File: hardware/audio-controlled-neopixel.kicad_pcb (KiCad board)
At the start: 2 copper layers, 96 x 56 mm, 61 parts, among them J1 Phoenix MPT, J2 KF2EDGK, J3 KF2EDGK, J4 KF2EDGK, J5 Conn_01x01_Female, J6 Conn_01x01_Female, J7 Conn_01x01_Female, J8 Conn_01x01_Female, SW1 SW_SPST, U1 LM324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

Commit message: minor PCB clean up
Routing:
- net -12V: track 198.4 -> 204.7 mm
- net Net-(C2-Pad1): track 23.4 -> 24.6 mm
- net +12V: track 138.8 -> 139.8 mm
- net Net-(C1-Pad1): track 29.2 -> 29.8 mm
- net /Buf_input: track 35.6 -> 36.1 mm
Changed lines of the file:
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@@
     (thickness 1.6)
     (drawings 23)
-    (tracks 331)
+    (tracks 326)
     (zones 0)
     (modules 61)
@@
   (segment (start 48.26 51.308) (end 48.26 52.672) (width 0.5) (layer F.Cu) (net 2))
   (segment (start 48.006 51.054) (end 48.26 51.308) (width 0.5) (layer F.Cu) (net 2))
-  (segment (start 44.102 52.672) (end 46.99 52.672) (width 0.5) (layer F.Cu) (net 2))
-  (segment (start 41.148 67.818) (end 41.148 55.626) (width 0.5) (layer F.Cu) (net 2))
-  (segment (start 41.148 55.626) (end 44.102 52.672) (width 0.5) (layer F.Cu) (net 2))
+  (segment (start 42.07 52.672) (end 46.99 52.672) (width 0.5) (layer F.Cu) (net 2))
+  (segment (start 41.148 67.818) (end 41.148 53.594) (width 0.5) (layer F.Cu) (net 2))
+  (segment (start 41.148 53.594) (end 42.07 52.672) (width 0.5) (layer F.Cu) (net 2))
   (segment (start 54.61 52.672) (end 54.61 51.422) (width 0.5) (layer F.Cu) (net 3))
   (segment (start 53.34 51.422) (end 53.708 51.054) (width 0.5) (layer F.Cu) (net 3))
@@
   (segment (start 46.736 66.518) (end 43.434 63.216) (width 0.5) (layer F.Cu) (net 3))
   (segment (start 46.736 67.818) (end 46.736 66.518) (width 0.5) (layer F.Cu) (net 3))
-  (segment (start 43.434 63.216) (end 43.434 56.134) (width 0.5) (layer F.Cu) (net 3))
-  (segment (start 43.434 56.134) (end 45.212 54.356) (width 0.5) (layer F.Cu) (net 3))
-  (segment (start 45.212 54.356) (end 52.906 54.356) (width 0.5) (layer F.Cu) (net 3))
+  (segment (start 43.434 63.216) (end 43.434 55.118) (width 0.5) (layer F.Cu) (net 3))
+  (segment (start 43.434 55.118) (end 44.196 54.356) (width 0.5) (layer F.Cu) (net 3))
+  (segment (start 44.196 54.356) (end 52.906 54.356) (width 0.5) (layer F.Cu) (net 3))
   (segment (start 52.906 54.356) (end 53.34 53.922) (width 0.5) (layer F.Cu) (net 3))
   (segment (start 67.915 58.674) (end 67.945 58.704) (width 0.5) (layer F.Cu) (net 4))
@@
   (segment (start 46.9085 57.9905) (end 46.99 58.072) (width 0.5) (layer F.Cu) (net 5))
   (segment (start 44.958 57.9905) (end 46.9085 57.9905) (width 0.5) (layer F.Cu) (net 5))
-  (segment (start 61.6435 55.5475) (end 61.6435 56.896) (width 0.5) (layer F.Cu) (net 5))
-  (segment (start 61.214 55.118) (end 61.6435 55.5475) (width 0.5) (layer F.Cu) (net 5))
-  (segment (start 48.694 55.118) (end 61.214 55.118) (width 0.5) (layer F.Cu) (net 5))
-  (segment (start 46.99 58.072) (end 46.99 56.822) (width 0.5) (layer F.Cu) (net 5))
-  (segment (start 46.99 56.822) (end 48.694 55.118) (width 0.5) (layer F.Cu) (net 5))
   (segment (start 65.913 56.896) (end 66.04 57.023) (width 0.5) (layer F.Cu) (net 5))
   (segment (start 61.6435 56.896) (end 65.913 56.896) (width 0.5) (layer F.Cu) (net 5))
+  (segment (start 61.6435 55.5475) (end 61.6435 56.896) (width 0.5) (layer F.Cu) (net 5))
+  (segment (start 61.214 55.118) (end 61.6435 55.5475) (width 0.5) (layer F.Cu) (net 5))
+  (segment (start 47.752 55.118) (end 61.214 55.118) (width 0.5) (layer F.Cu) (net 5))
+  (segment (start 46.99 58.072) (end 46.99 55.88) (width 0.5) (layer F.Cu) (net 5))
+  (segment (start 46.99 55.88) (end 47.752 55.118) (width 0.5) (layer F.Cu) (net 5))
   (segment (start 83.057 83.7385) (end 83.1065 83.788) (width 0.5) (layer F.Cu) (net 6))
   (segment (start 83.057 81.375) (end 83.057 83.7385) (width 0.5) (layer F.Cu) (net 6))
@@
   (segment (start 79.248 70.9445) (end 79.248 69.85) (width 0.5) (layer F.Cu) (net 21))
   (segment (start 79.248 69.85) (end 79.248 67.978) (width 0.5) (layer F.Cu) (net 21))
-  (via (at 63.246 30.734) (size 0.8) (drill 0.4) (layers F.Cu B.Cu) (net 21))
   (segment (start 39.37 42.164) (end 50.8 30.734) (width 0.5) (layer B.Cu) (net 21))
   (segment (start 39.37 56.388) (end 39.37 42.164) (width 0.5) (layer B.Cu) (net 21))
@@
   (segment (start 62.680315 30.734) (end 63.246 30.734) (width 0.5) (layer B.Cu) (net 21))
   (via (at 77.47 73.152) (size 0.8) (drill 0.4) (layers F.Cu B.Cu) (net 21))
-  (segment (start 63.645999 31.133999) (end 63.246 30.734) (width 0.5) (layer F.Cu) (net 21))
-  (segment (start 69.088 37.338) (end 69.088 39.116) (width 0.5) (layer F.Cu) (net 21))
-  (segment (start 68.326 39.878) (end 64.77 39.878) (width 0.5) (layer F.Cu) (net 21))
-  (segment (start 64.77 39.878) (end 64.262 39.37) (width 0.5) (layer F.Cu) (net 21))
-  (segment (start 64.262 39.37) (end 64.262 31.75) (width 0.5) (layer F.Cu) (net 21))
-  (segment (start 64.262 31.75) (end 63.645999 31.133999) (width 0.5) (layer F.Cu) (net 21))
-  (segment (start 115.824 34.414208) (end 115.445792 34.036) (width 0.5) (layer F.Cu) (net 21))
-  (segment (start 115.824 35.687) (end 115.824 34.414208) (width 0.5) (layer F.Cu) (net 21))
-  (segment (start 115.445792 34.036) (end 80.518 34.036) (width 0.5) (layer F.Cu) (net 21))
-  (segment (start 80.518 34.036) (end 74.676 39.878) (width 0.5) (layer F.Cu) (net 21))
-  (segment (start 69.088 39.116) (end 69.088 39.878) (width 0.5) (layer F.Cu) (net 21))
-  (segment (start 74.676 39.878) (end 69.088 39.878) (width 0.5) (layer F.Cu) (net 21))
-  (segment (start 69.088 39.878) (end 68.326 39.878) (width 0.5) (layer F.Cu) (net 21))
   (segment (start 39.37 72.898) (end 39.37 56.388) (width 0.5) (layer B.Cu) (net 21))
   (segment (start 50.8 84.328) (end 39.37 72.898) (width 0.5) (layer B.Cu) (net 21))
@@
   (segment (start 79.248 70.9445) (end 77.6455 70.9445) (width 0.5) (layer F.Cu) (net 21))
   (segment (start 77.6455 70.9445) (end 77.47 71.12) (width 0.5) (layer F.Cu) (net 21))
+  (segment (start 115.824 31.242) (end 115.824 35.687) (width 0.5) (layer B.Cu) (net 21))
+  (segment (start 115.316 30.734) (end 115.824 31.242) (width 0.5) (layer B.Cu) (net 21))
+  (via (at 74.422 30.734) (size 0.8) (drill 0.4) (layers F.Cu B.Cu) (net 21))
+  (segment (start 63.246 30.734) (end 74.422 30.734) (width 0.5) (layer B.Cu) (net 21))
+  (segment (start 74.422 30.734) (end 115.316 30.734) (width 0.5) (layer B.Cu) (net 21))
+  (segment (start 74.422 38.862) (end 74.422 30.734) (width 0.5) (layer F.Cu) (net 21))
+  (segment (start 73.152 40.132) (end 74.422 38.862) (width 0.5) (layer F.Cu) (net 21))
+  (segment (start 69.85 40.132) (end 73.152 40.132) (width 0.5) (layer F.Cu) (net 21))
+  (segment (start 69.088 37.338) (end 69.088 39.37) (width 0.5) (layer F.Cu) (net 21))
+  (segment (start 69.088 39.37) (end 69.85 40.132) (width 0.5) (layer F.Cu) (net 21))
   (segment (start 50.8 50.7215) (end 50.8 52.672) (width 0.5) (layer F.Cu) (net 22))
   (segment (start 50.8 48.9435) (end 50.8 50.7215) (width 0.5) (layer F.Cu) (net 22))
-  (segment (start 65.278 37.338) (end 66.548 37.338) (width 0.5) (layer B.Cu) (net 22))
-  (segment (start 109.471208 35.687) (end 105.534208 31.75) (width 0.5) (layer B.Cu) (net 22))
-  (segment (start 110.744 35.687) (end 109.471208 35.687) (width 0.5) (layer B.Cu) (net 22))
-  (segment (start 105.534208 31.75) (end 65.786 31.75) (width 0.5) (layer B.Cu) (net 22))
   (segment (start 65.786 31.75) (end 64.516 33.02) (width 0.5) (layer B.Cu) (net 22))
-  (segment (start 64.516 33.02) (end 64.516 36.576) (width 0.5) (layer B.Cu) (net 22))
-  (segment (start 64.516 36.576) (end 65.278 37.338) (width 0.5) (layer B.Cu) (net 22))
-  (segment (start 66.548 37.338) (end 66.548 39.624) (width 0.5) (layer B.Cu) (net 22))
   (via (at 50.8 50.7215) (size 0.8) (drill 0.4) (layers F.Cu B.Cu) (net 22))
   (segment (start 40.5615 50.7215) (end 50.8 50.7215) (width 0.5) (layer B.Cu) (net 22))
@@
   (segment (start 78.0265 59.7385) (end 77.47 59.182) (width 0.5) (layer F.Cu) (net 22))
   (segment (start 77.47 59.182) (end 77.47 56.896) (width 0.5) (layer F.Cu) (net 22))
-  (segment (start 70.104 43.18) (end 70.104 55.372) (width 0.5) (layer B.Cu) (net 22))
-  (segment (start 66.548 39.624) (end 70.104 43.18) (width 0.5) (layer B.Cu) (net 22))
-  (segment (start 71.628 56.896) (end 77.47 56.896) (width 0.5) (layer B.Cu) (net 22))
-  (segment (start 70.104 55.372) (end 71.628 56.896) (width 0.5) (layer B.Cu) (net 22))
+  (segment (start 77.47 56.896) (end 77.47 51.054) (width 0.5) (layer B.Cu) (net 22))
+  (segment (start 80.518 48.006) (end 80.518 31.75) (width 0.5) (layer B.Cu) (net 22))
+  (segment (start 77.47 51.054) (end 80.518 48.006) (width 0.5) (layer B.Cu) (net 22))
+  (segment (start 80.518 31.75) (end 65.786 31.75) (width 0.5) (layer B.Cu) (net 22))
+  (segment (start 65.024 37.338) (end 66.548 37.338) (width 0.5) (layer B.Cu) (net 22))
+  (segment (start 64.516 33.02) (end 64.516 36.83) (width 0.5) (layer B.Cu) (net 22))
+  (segment (start 64.516 36.83) (end 65.024 37.338) (width 0.5) (layer B.Cu) (net 22))
+  (segment (start 109.982 31.75) (end 80.518 31.75) (width 0.5) (layer B.Cu) (net 22))
+  (segment (start 110.744 35.687) (end 110.744 32.512) (width 0.5) (layer B.Cu) (net 22))
+  (segment (start 110.744 32.512) (end 109.982 31.75) (width 0.5) (layer B.Cu) (net 22))
   (segment (start 84.201 56.896) (end 85.98 56.896) (width 0.5) (layer F.Cu) (net 23))
   (segment (start 83.058 58.039) (end 84.201 56.896) (width 0.5) (layer F.Cu) (net 23))

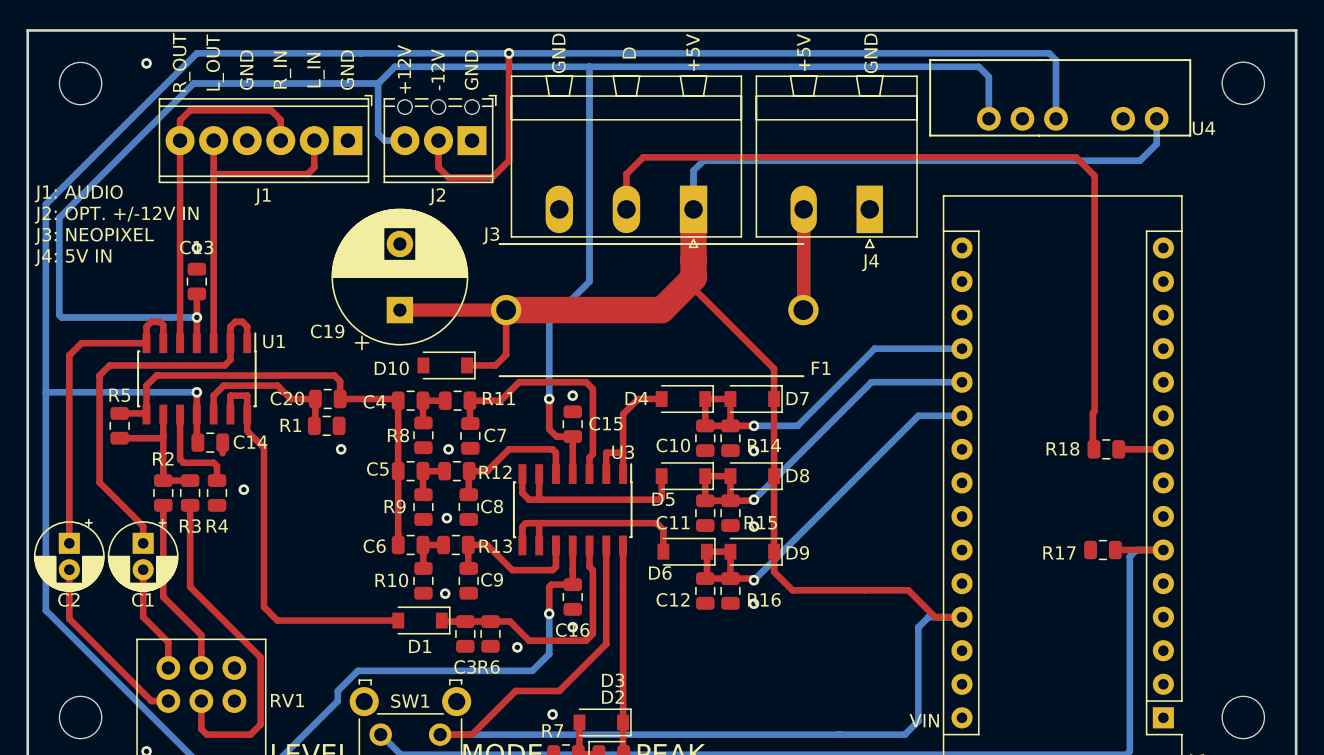
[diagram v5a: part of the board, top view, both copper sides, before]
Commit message: update schematic to use 3.5mm audio I/O
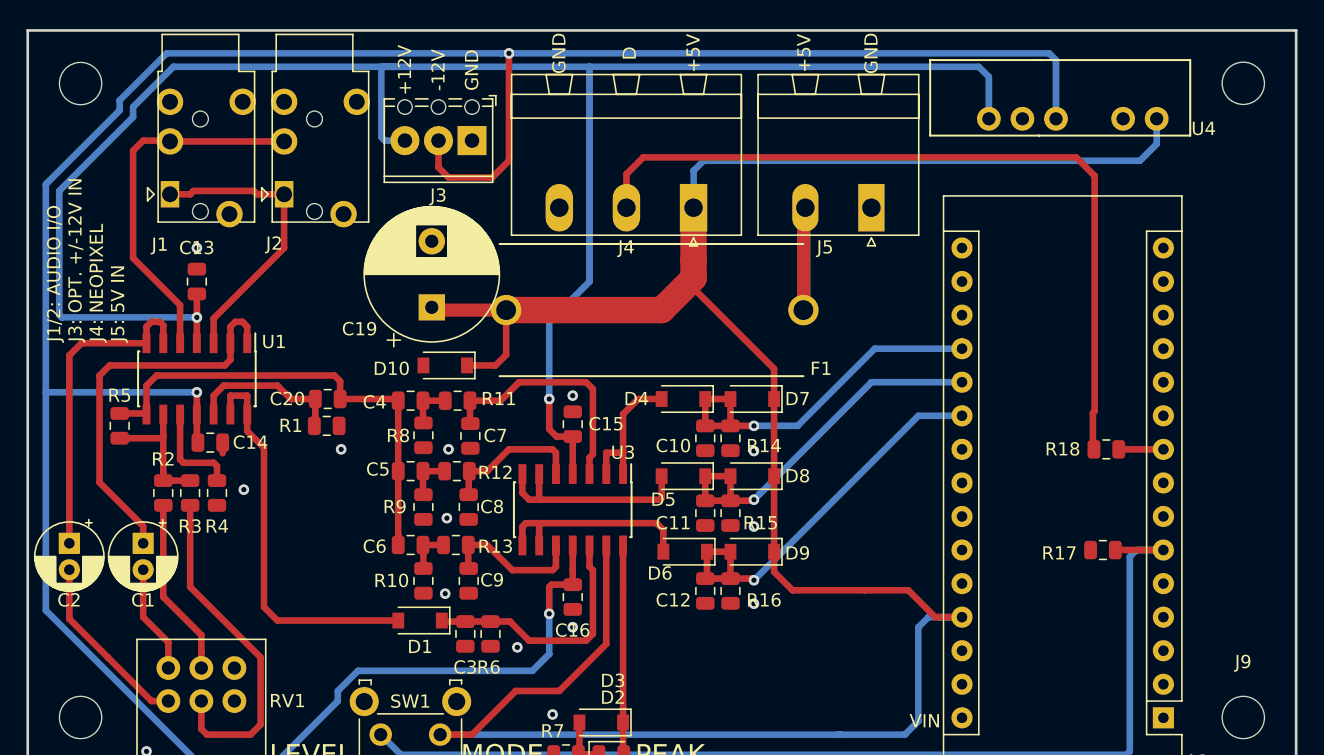
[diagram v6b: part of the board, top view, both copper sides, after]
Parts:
- added J9: Conn_01x01_Female, MountingHole:MountingHole_3.2mm_M3, F.Cu at (130.0, 81.0)
- J1: value Phoenix MPT -> AudioJack3_Ground; footprint TerminalBlock_Phoenix:TerminalBlock_Phoenix_MPT-0,5-6-2.54_1x06_P2.54mm_Horizontal -> Footprints:Jack_3.5mm_PJ320E_Horizontal
- J2: value KF2EDGK -> AudioJack3_Ground; footprint TerminalBlock_Phoenix:TerminalBlock_Phoenix_MPT-0,5-3-2.54_1x03_P2.54mm_Horizontal -> Footprints:Jack_3.5mm_PJ320E_Horizontal
- J3: footprint Connector_Phoenix_MSTB:PhoenixContact_MSTBA_2,5_3-G-5,08_1x03_P5.08mm_Horizontal -> TerminalBlock_Phoenix:TerminalBlock_Phoenix_MPT-0,5-3-2.54_1x03_P2.54mm_Horizontal
- J4: footprint Connector_Phoenix_MSTB:PhoenixContact_MSTBA_2,5_2-G_1x02_P5.00mm_Horizontal -> Connector_Phoenix_MSTB:PhoenixContact_MSTBA_2,5_3-G-5,08_1x03_P5.08mm_Horizontal
- J5: value Conn_01x01_Female -> KF2EDGK; footprint MountingHole:MountingHole_3.2mm_M3 -> Connector_Phoenix_MSTB:PhoenixContact_MSTBA_2,5_2-G_1x02_P5.00mm_Horizontal
- moved J5 47.8 mm to (101.9, 42.4), turned to 180 degrees
- moved J3 17.6 mm to (71.6, 37.3)
- moved J2 14.8 mm to (57.4, 41.4), turned to 0 degrees
- moved J1 14.1 mm to (48.8, 41.4), turned to 0 degrees
- moved J4 13.3 mm to (88.4, 42.4)
- moved C19 2.42 mm to (68.6, 50.0)
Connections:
- J1 pad 2: /Input_L -> Net-(J1-Pad2)
- J1 pad 4: GND -> /Input_L
- J1 pad 5: /Input_L -> GND
- J1 pad 6: /Input_R -> (no net)
- J2 pad 2: -12V -> Net-(J2-Pad2)
- J2 pad 3: +12V -> /Input_R
- J3 pad 1: +5V -> GND
- J3 pad 2: /Neopixel -> -12V
- J3 pad 3: GND -> +12V
- J4 pad 1: GND -> +5V
- J4 pad 2: Net-(F1-Pad2) -> /Neopixel
- J5 pad 1: Net-(J5-Pad1) -> GND
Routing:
- net +12V: track 139.8 -> 143.6 mm
- net /Input_L: track 25.2 -> 22.3 mm
- net +5V: track 187.0 -> 184.6 mm
- net -12V: track 204.7 -> 206.1 mm
- net /Input_R: track 26.7 -> 27.8 mm
- net GND: track 0.80 -> 1.31 mm, vias 15 -> 14
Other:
- board text added: "J1/2: AUDIO I/O J3: OPT. +/-12V IN J4: NEOPIXEL J5: 5V IN"
- board text removed: "J1: AUDIO J2: OPT. +/-12V IN J3: NEOPIXEL J4: 5V IN"
- board text removed: "L_IN"
- board text removed: "L_OUT"
- board text removed: "R_IN"
- board text removed: "R_OUT"

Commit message: clean up schematic and PCB
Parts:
- removed C16: 100n, Capacitor_SMD:C_0805_2012Metric
- moved D10 7.38 mm to (70.1, 47.0)
- moved C19 3.56 mm to (65.0, 50.0), turned to 180 degrees
- moved C14 0.25 mm to (51.8, 60.5)
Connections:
- U3 pad 11: -12V -> GND
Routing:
- net -12V: track 206.1 -> 133.0 mm, vias 3 -> 2
- net +5V: track 184.6 -> 167.1 mm, vias 0 -> 2
- net Net-(C3-Pad1): track 19.1 -> 16.8 mm
- net GND: track 1.31 -> 3.18 mm, vias 14 -> 18

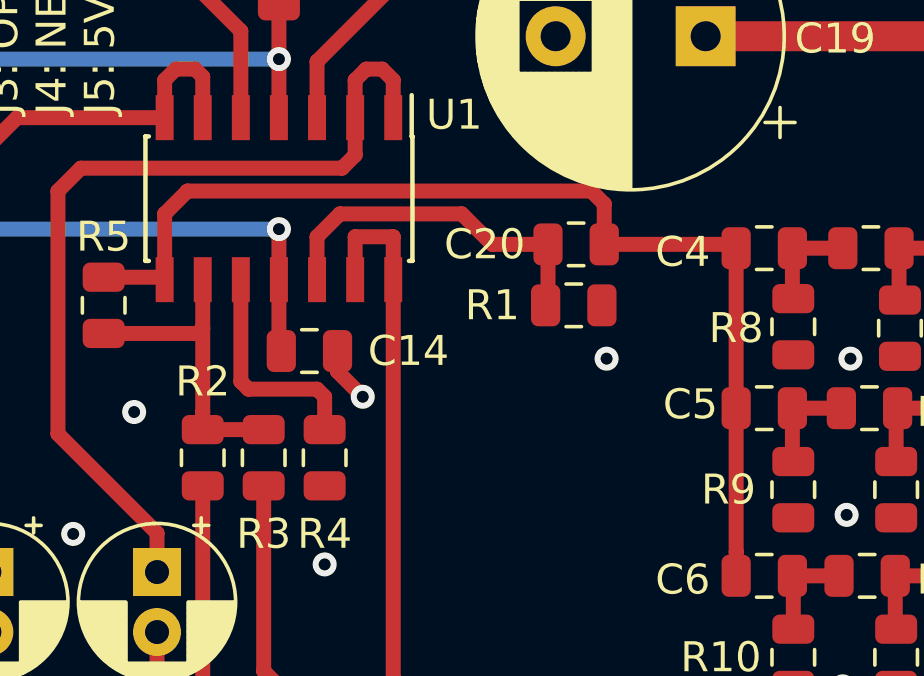
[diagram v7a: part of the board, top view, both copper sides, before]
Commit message: add attenuator for peak level calibration
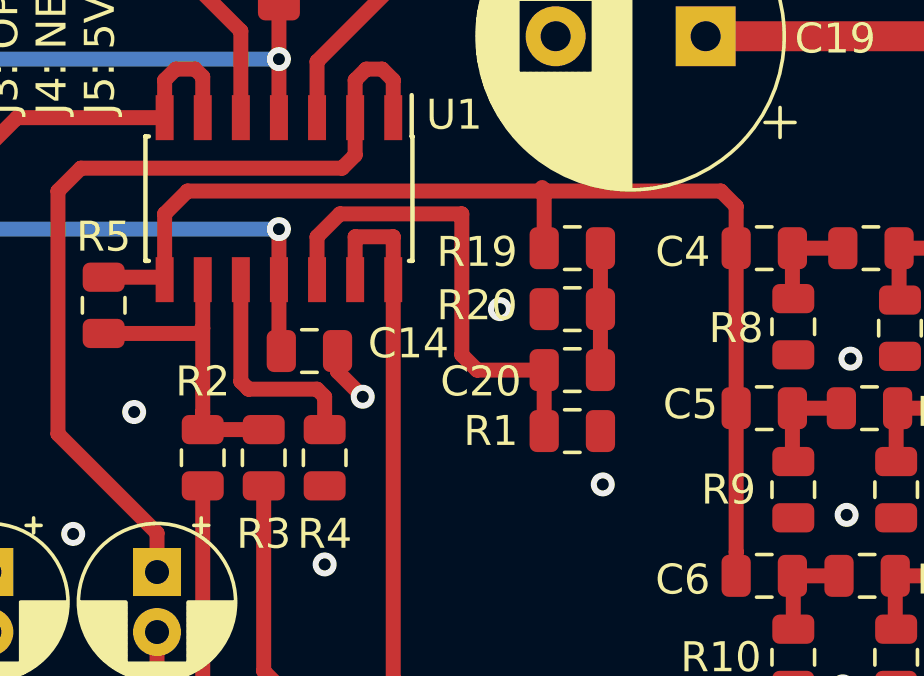
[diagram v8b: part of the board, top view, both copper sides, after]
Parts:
- added R19: 100K, Resistor_SMD:R_0805_2012Metric, F.Cu at (60.6, 57.0)
- added R20: 100K, Resistor_SMD:R_0805_2012Metric, F.Cu at (60.6, 59.1)
- moved C20 4.19 mm to (60.6, 61.1)
- moved R1 4.19 mm to (60.6, 63.1)
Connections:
- C20 pad 2: /Buf_input -> Net-(C20-Pad2)
- J1 pad 2: Net-(J1-Pad2) -> (no net)
- J1 pad 3: /Input_R -> (no net)
- J1 pad 4: /Input_L -> (no net)
- J1 pad 5: GND -> (no net)
- J2 pad 2: Net-(J2-Pad2) -> (no net)
- J2 pad 3: /Input_R -> (no net)
- J2 pad 4: /Input_L -> (no net)
- J2 pad 5: GND -> (no net)
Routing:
- net Net-(C20-Pad1): track 11.9 -> 16.3 mm
- net Net-(C20-Pad2): track 0.00 -> 4.06 mm
- net /Buf_input: track 36.1 -> 38.3 mm
- net GND: track 3.18 -> 2.67 mm, vias 18 -> 19
- net (no net): track 0.00 -> 0.51 mm
